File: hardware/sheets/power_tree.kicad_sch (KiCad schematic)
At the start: 56 parts, among them Q201 AO3401A, Q202 AO3400A, Q203 AO3401A, Q204 AO3400A, SW201 PCM12SMTR, U201 TPS63802, U202 TPS61023

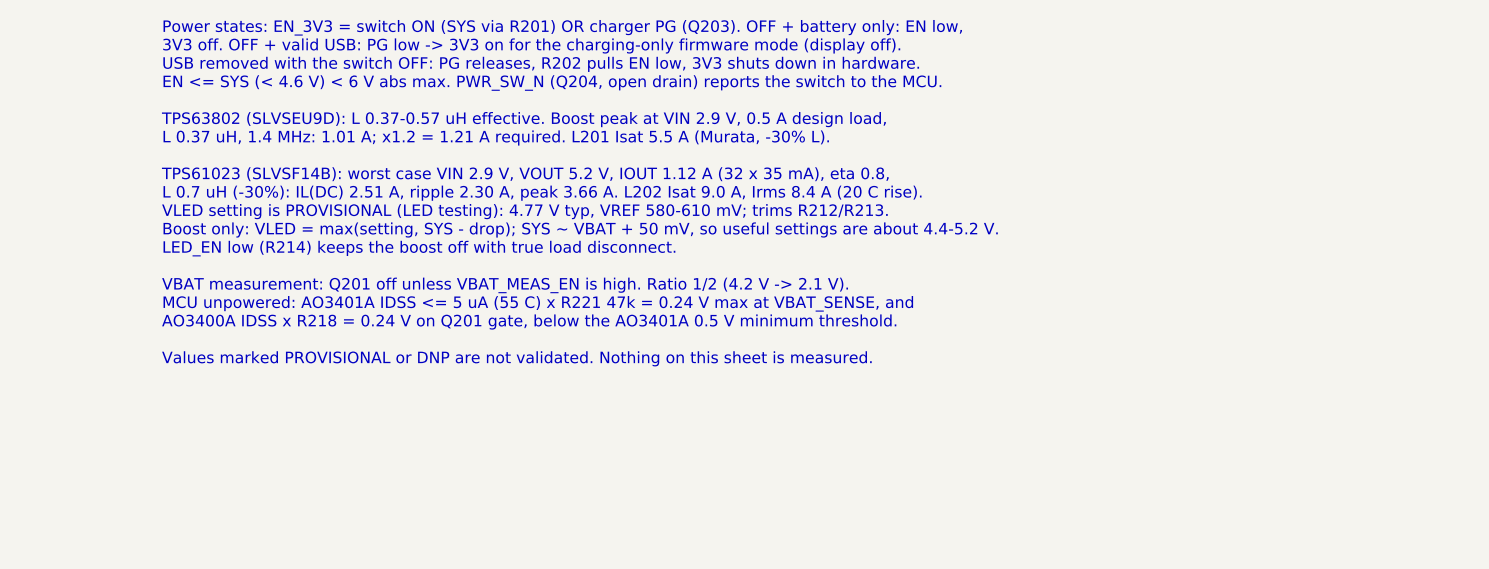
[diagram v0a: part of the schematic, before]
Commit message: hw: use single-sided assembly with a through-hole battery header and low-profile inductors (#11)
* hw: use a through-hole side-entry battery header

The board is assembled on one side only, so the battery header can no
longer be an SMT part on the rear. J302 becomes a JST S2B-PH-K-S
through-hole side-entry header: its body sits on the rear beside the
pack's lead exit and its pins are soldered from the front, outside the
LED field. The footprint matches JST's through-hole layout (circuit 1
position, 2.0 mm pitch, 0.75 mm drill).

The symbol becomes a plain two-pin connector because the part has no
mounting pads. Pin 1 stays BAT- and pin 2 BAT+. An Assembly field marks
the part as hand-soldered after assembly unless the assembler confirms
rear insertion.

* hw: use 2.1 mm XGL4020 inductors for the LED rail and charger

With every part on the front, part height adds directly to the badge
thickness. The 3.1 mm XEL4030 on the LED boost (L202) and charger (L301)
becomes a Coilcraft XGL4020-102MEC, 2.10 mm max, with the same 0.98 x
3.4 mm land pattern at 2.37 mm centres.

The worst-case boost peak is 2.94 A with the 18.0 mA column cap (2.9 V
in, 5.33 V out, 0.66 A, -20 % inductance tolerance, -20 % switching
frequency), below the 3.8 A rating for a 10 % inductance drop. The
earlier 3.66 A figure assumed 35 mA columns. The charger peaks at
2.76 A at the 1.5 A input limit. Current-limit cases stay below the
30 % drop point. These are calculations, not measurements.

* docs: record dual-orientation wear and single-sided assembly

ADR 0009: the badge is worn landscape or portrait, with firmware
rotating the content from the IMU and QR mode keeping its orientation
until it is left. Magnetic and lanyard mounting are both required; the
carrier takes the lanyard load.

ADR 0010: all components are on the front and the rear holds only the
battery, the battery connector body and the carrier. Thickness targets
become regional: about 12 mm over the LED field, 13.5 mm over the
electron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
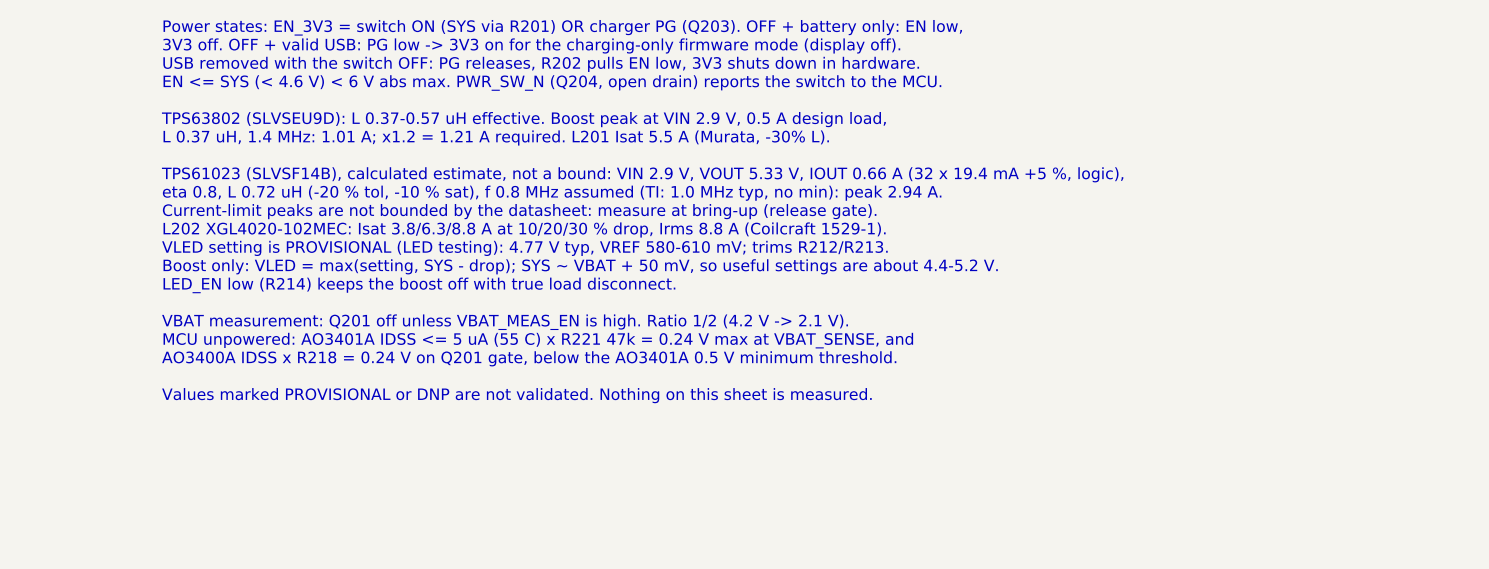
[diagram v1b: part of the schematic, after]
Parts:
- L202: footprint smart-led-badge:L_Coilcraft_XEL4030 -> smart-led-badge:L_Coilcraft_XGL4020; LCSC C5441341 -> C5357696; MPN XEL4030-102MEC -> XGL4020-102MEC
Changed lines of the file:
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@@
 		)
 	)
-	(text "Regulators and power tree (Rev A) - design notes\n\nPower states: EN_3V3 = switch ON (SYS via R201) OR charger PG (Q203). OFF + battery only: EN low,\n3V3 off. OFF + valid USB: PG low -> 3V3 on for the charging-only firmware mode (display off).\nUSB removed with the switch OFF: PG releases, R202 pulls EN low, 3V3 shuts down in hardware.\nEN <= SYS (< 4.6 V) < 6 V abs max. PWR_SW_N (Q204, open drain) reports the switch to the MCU.\n\nTPS63802 (SLVSEU9D): L 0.37-0.57 uH effective. Boost peak at VIN 2.9 V, 0.5 A design load,\nL 0.37 uH, 1.4 MHz: 1.01 A; x1.2 = 1.21 A required. L201 Isat 5.5 A (Murata, -30% L).\n\nTPS61023 (SLVSF14B): worst case VIN 2.9 V, VOUT 5.2 V, IOUT 1.12 A (32 x 35 mA), eta 0.8,\nL 0.7 uH (-30%): IL(DC) 2.51 A, ripple 2.30 A, peak 3.66 A. L202 Isat 9.0 A, Irms 8.4 A (20 C rise).\nVLED setting is PROVISIONAL (LED testing): 4.77 V typ, VREF 580-610 mV; trims R212/R213.\nBoost only: VLED = max(setting, SYS - drop); SYS ~ VBAT + 50 mV, so useful settings are about 4.4-5.2 V.\nLED_EN low (R214) keeps the boost off with true load disconnect.\n\nVBAT measurement: Q201 off unless VBAT_MEAS_EN is high. Ratio 1/2 (4.2 V -> 2.1 V).\nMCU unpowered: AO3401A IDSS <= 5 uA (55 C) x R221 47k = 0.24 V max at VBAT_SENSE, and\nAO3400A IDSS x R218 = 0.24 V on Q201 gate, below the AO3401A 0.5 V minimum threshold.\n\nValues marked PROVISIONAL or DNP are not validated. Nothing on this sheet is measured."
+	(text "Regulators and power tree (Rev A) - design notes\n\nPower states: EN_3V3 = switch ON (SYS via R201) OR charger PG (Q203). OFF + battery only: EN low,\n3V3 off. OFF + valid USB: PG low -> 3V3 on for the charging-only firmware mode (display off).\nUSB removed with the switch OFF: PG releases, R202 pulls EN low, 3V3 shuts down in hardware.\nEN <= SYS (< 4.6 V) < 6 V abs max. PWR_SW_N (Q204, open drain) reports the switch to the MCU.\n\nTPS63802 (SLVSEU9D): L 0.37-0.57 uH effective. Boost peak at VIN 2.9 V, 0.5 A design load,\nL 0.37 uH, 1.4 MHz: 1.01 A; x1.2 = 1.21 A required. L201 Isat 5.5 A (Murata, -30% L).\n\nTPS61023 (SLVSF14B), calculated estimate, not a bound: VIN 2.9 V, VOUT 5.33 V, IOUT 0.66 A (32 x 19.4 mA +5 %, logic),\neta 0.8, L 0.72 uH (-20 % tol, -10 % sat), f 0.8 MHz assumed (TI: 1.0 MHz typ, no min): peak 2.94 A.\nCurrent-limit peaks are not bounded by the datasheet: measure at bring-up (release gate).\nL202 XGL4020-102MEC: Isat 3.8/6.3/8.8 A at 10/20/30 % drop, Irms 8.8 A (Coilcraft 1529-1).\nVLED setting is PROVISIONAL (LED testing): 4.77 V typ, VREF 580-610 mV; trims R212/R213.\nBoost only: VLED = max(setting, SYS - drop); SYS ~ VBAT + 50 mV, so useful settings are about 4.4-5.2 V.\nLED_EN low (R214) keeps the boost off with true load disconnect.\n\nVBAT measurement: Q201 off unless VBAT_MEAS_EN is high. Ratio 1/2 (4.2 V -> 2.1 V).\nMCU unpowered: AO3401A IDSS <= 5 uA (55 C) x R221 47k = 0.24 V max at VBAT_SENSE, and\nAO3400A IDSS x R218 = 0.24 V on Q201 gate, below the AO3401A 0.5 V minimum threshold.\n\nValues marked PROVISIONAL or DNP are not validated. Nothing on this sheet is measured."
 		(exclude_from_sim no)
 		(at 299.72 152.4 0)
@@
 			)
 		)
-		(property "Footprint" "smart-led-badge:L_Coilcraft_XEL4030"
+		(property "Footprint" "smart-led-badge:L_Coilcraft_XGL4020"
 			(at 101.6 99.06 0)
 			(hide yes)
@@
 			)
 		)
-		(property "MPN" "XEL4030-102MEC"
+		(property "MPN" "XGL4020-102MEC"
 			(at 101.6 99.06 0)
 			(hide yes)
@@
 			)
 		)
-		(property "LCSC" "C5441341"
+		(property "LCSC" "C5357696"
 			(at 101.6 99.06 0)
 			(hide yes)
